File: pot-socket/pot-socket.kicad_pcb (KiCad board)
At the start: 2 copper layers, 18 x 20 mm, 2 parts, among them J1 Conn_01x03

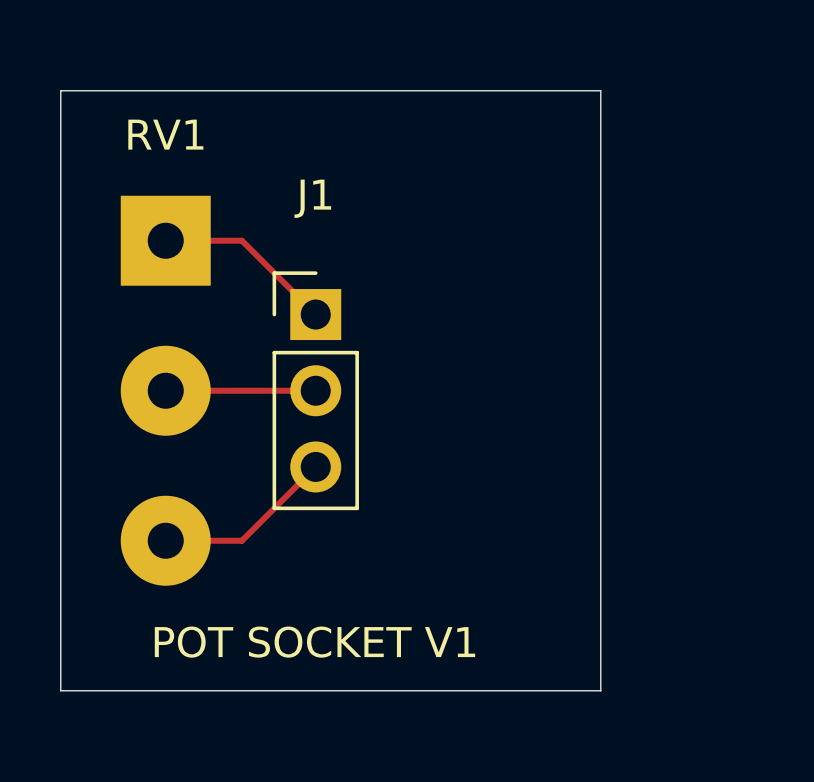
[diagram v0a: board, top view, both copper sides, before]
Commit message: Freecad design for pot socket
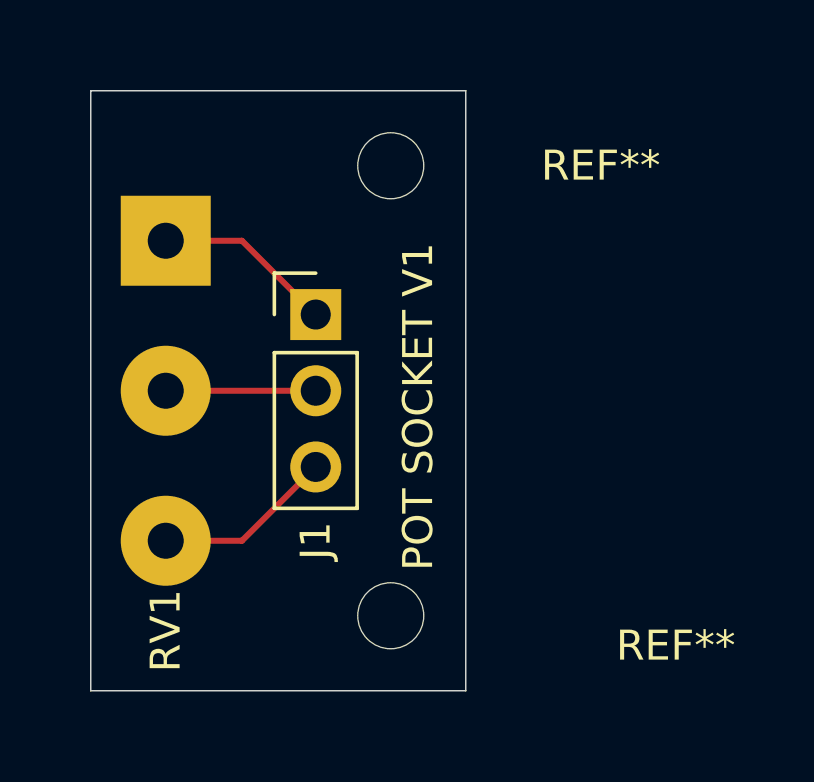
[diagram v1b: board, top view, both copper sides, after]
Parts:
- added REF**: MountingHole_2.2mm_M2, MountingHole:MountingHole_2.2mm_M2, F.Cu at (152.5, 92.5)
- added REF**: MountingHole_2.2mm_M2, MountingHole:MountingHole_2.2mm_M2, F.Cu at (152.5, 107.5)
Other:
- board size 18 x 20 mm -> 12.5 x 20 mm
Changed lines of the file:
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@@
 		(tags "Potentiometer horizontal Alps RK163 Single")
 		(property "Reference" "RV1"
-			(at 0 -3.5 180)
+			(at 0 13 270)
 			(layer "F.SilkS")
 			(effects
@@
 			)
 		)
+	)
+	(footprint "MountingHole:MountingHole_2.2mm_M2"
+		(layer "F.Cu")
+		(at 152.5 92.5)
+		(descr "Mounting Hole 2.2mm, M2, no annular, generated by kicad-footprint-generator mountinghole.py")
+		(tags "mountinghole M2")
+		(property "Reference" "REF**"
+			(at 7 0 0)
+			(layer "F.SilkS")
+			(effects
+				(font
+					(size 1 1)
+					(thickness 0.15)
+				)
+			)
+		)
+		(property "Value" "MountingHole_2.2mm_M2"
+			(at 0 3.15 0)
+			(layer "F.Fab")
+			(effects
+				(font
+					(size 1 1)
+					(thickness 0.15)
+				)
+			)
+		)
+		(property "Datasheet" ""
+			(at 0 0 0)
+			(layer "F.Fab")
+			(hide yes)
+			(effects
+				(font
+					(size 1.27 1.27)
+					(thickness 0.15)
+				)
+			)
+		)
+		(property "Description" ""
+			(at 0 0 0)
+			(layer "F.Fab")
+			(hide yes)
+			(effects
+				(font
+					(size 1.27 1.27)
+					(thickness 0.15)
+				)
+			)
+		)
+		(attr exclude_from_pos_files exclude_from_bom)
+		(fp_circle
+			(center 0 0)
+			(end 2.2 0)
+			(stroke
+				(width 0.15)
+				(type solid)
+			)
+			(fill no)
+			(layer "Cmts.User")
+		)
+		(fp_circle
+			(center 0 0)
+			(end 2.45 0)
+			(stroke
+				(width 0.05)
+				(type solid)
+			)
+			(fill no)
+			(layer "F.CrtYd")
+		)
+		(fp_text user "${REFERENCE}"
+			(at 0 0 0)
+			(layer "F.Fab")
+			(effects
+				(font
+					(size 1 1)
+					(thickness 0.15)
+				)
+			)
+		)
+		(pad "" np_thru_hole circle
+			(at 0 0)
+			(size 2.2 2.2)
+			(drill 2.2)
+			(layers "*.Cu" "*.Mask")
+		)
+		(embedded_fonts no)
 	)
 	(footprint "Connector_PinHeader_2.54mm:PinHeader_1x03_P2.54mm_Vertical"
@@
 		(tags "Through hole pin header THT 1x03 2.54mm single row")
 		(property "Reference" "J1"
-			(at 0 -3.96 0)
+			(at 0 7.54 90)
 			(layer "F.SilkS")
 			(effects
@@
 		)
 	)
+	(footprint "MountingHole:MountingHole_2.2mm_M2"
+		(layer "F.Cu")
+		(at 152.5 107.5)
+		(descr "Mounting Hole 2.2mm, M2, no annular, generated by kicad-footprint-generator mountinghole.py")
+		(tags "mountinghole M2")
+		(property "Reference" "REF**"
+			(at 9.5 1 0)
+			(layer "F.SilkS")
+			(effects
+				(font
+					(size 1 1)
+					(thickness 0.15)
+				)
+			)
+		)
+		(property "Value" "MountingHole_2.2mm_M2"
+			(at 0 3.15 0)
+			(layer "F.Fab")
+			(effects
+				(font
+					(size 1 1)
+					(thickness 0.15)
+				)
+			)
+		)
+		(property "Datasheet" ""
+			(at 0 0 0)
+			(layer "F.Fab")
+			(hide yes)
+			(effects
+				(font
+					(size 1.27 1.27)
+					(thickness 0.15)
+				)
+			)
+		)
+		(property "Description" ""
+			(at 0 0 0)
+			(layer "F.Fab")
+			(hide yes)
+			(effects
+				(font
+					(size 1.27 1.27)
+					(thickness 0.15)
+				)
+			)
+		)
+		(attr exclude_from_pos_files exclude_from_bom)
+		(fp_circle
+			(center 0 0)
+			(end 2.2 0)
+			(stroke
+				(width 0.15)
+				(type solid)
+			)
+			(fill no)
+			(layer "Cmts.User")
+		)
+		(fp_circle
+			(center 0 0)
+			(end 2.45 0)
+			(stroke
+				(width 0.05)
+				(type solid)
+			)
+			(fill no)
+			(layer "F.CrtYd")
+		)
+		(fp_text user "${REFERENCE}"
+			(at 0 0 0)
+			(layer "F.Fab")
+			(effects
+				(font
+					(size 1 1)
+					(thickness 0.15)
+				)
+			)
+		)
+		(pad "" np_thru_hole circle
+			(at 0 0)
+			(size 2.2 2.2)
+			(drill 2.2)
+			(layers "*.Cu" "*.Mask")
+		)
+		(embedded_fonts no)
+	)
 	(gr_rect
-		(start 141.5 90)
-		(end 159.5 110)
+		(start 142.5 90)
+		(end 155 110)
 		(stroke
 			(width 0.05)
@@
 	)
 	(gr_text "POT SOCKET V1"
-		(at 144.5 109 0)
+		(at 154 106 90)
 		(layer "F.SilkS")
 		(effects

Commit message: Update pot socket model
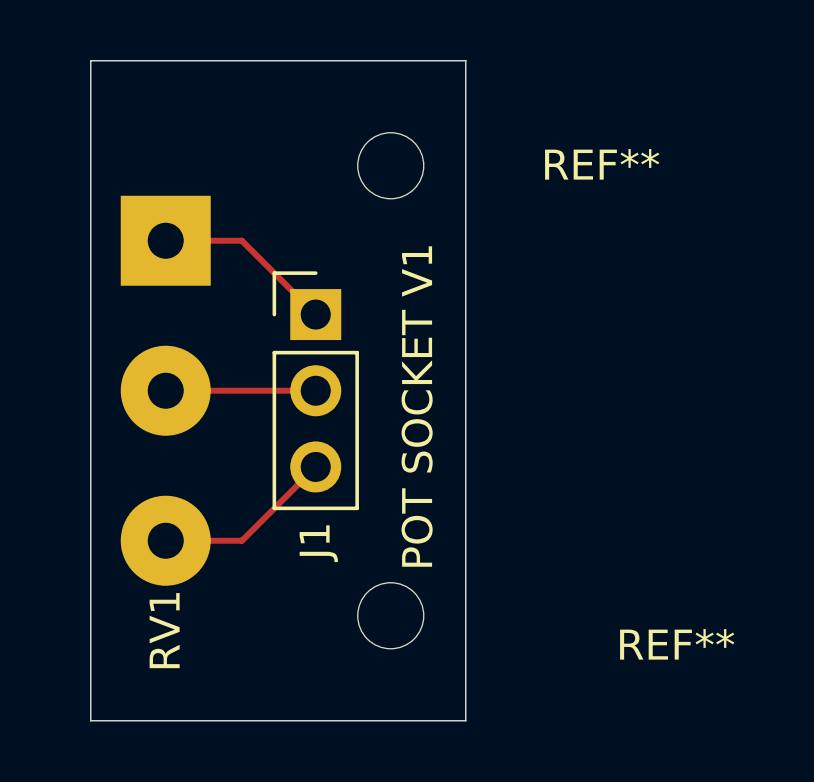
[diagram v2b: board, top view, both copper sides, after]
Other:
- board size 12.5 x 20 mm -> 12.5 x 22 mm
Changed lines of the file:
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@@
 	)
 	(gr_rect
-		(start 142.5 90)
-		(end 155 110)
+		(start 142.5 89)
+		(end 155 111)
 		(stroke
 			(width 0.05)

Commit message: Update pot socket pcb
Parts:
- moved RV1 2.50 mm to (147.5, 95.0)
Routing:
- net Net-(J1-Pin_3): track 6.02 -> 3.52 mm
- net Net-(J1-Pin_1): track 6.02 -> 3.52 mm
- net Net-(J1-Pin_2): track 5.00 -> 2.50 mm
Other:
- board size 12.5 x 22 mm -> 10.5 x 22 mm
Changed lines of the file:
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@@
 	(footprint "Potentiometer_THT:Potentiometer_Alps_RK163_Single_Horizontal"
 		(layer "F.Cu")
-		(at 145 95)
+		(at 147.5 95)
 		(descr "1110U1Q 1110TNP 1110U2A 1110U0Q Potentiometer, horizontal, Alps RK163 Single, https://tech.alpsalpine.com/prod/e/pdf/potentiometer/rotarypotentiometers/rk16/rk16.pdf")
 		(tags "Potentiometer horizontal Alps RK163 Single")
 		(property "Reference" "RV1"
-			(at 0 13 270)
+			(at 0 13.5 270)
 			(layer "F.SilkS")
 			(effects
@@
 		(attr through_hole)
 		(fp_line
-			(start -1.38 -1.38)
-			(end 0 -1.38)
-			(stroke
-				(width 0.12)
-				(type solid)
-			)
-			(layer "F.SilkS")
-		)
-		(fp_line
-			(start -1.38 0)
-			(end -1.38 -1.38)
-			(stroke
-				(width 0.12)
-				(type solid)
-			)
-			(layer "F.SilkS")
-		)
-		(fp_line
-			(start -1.38 1.27)
-			(end -1.38 6.46)
-			(stroke
-				(width 0.12)
-				(type solid)
-			)
-			(layer "F.SilkS")
-		)
-		(fp_line
-			(start -1.38 1.27)
-			(end 1.38 1.27)
-			(stroke
-				(width 0.12)
-				(type solid)
-			)
-			(layer "F.SilkS")
-		)
-		(fp_line
-			(start -1.38 6.46)
-			(end 1.38 6.46)
-			(stroke
-				(width 0.12)
-				(type solid)
-			)
-			(layer "F.SilkS")
-		)
-		(fp_line
-			(start 1.38 1.27)
-			(end 1.38 6.46)
-			(stroke
-				(width 0.12)
-				(type solid)
-			)
-			(layer "F.SilkS")
-		)
-		(fp_line
 			(start -1.77 -1.77)
 			(end -1.77 6.85)
@@
 			)
 			(layer "F.CrtYd")
-		)
-		(fp_line
-			(start -1.27 -0.635)
-			(end -0.635 -1.27)
-			(stroke
-				(width 0.1)
-				(type solid)
-			)
-			(layer "F.Fab")
-		)
-		(fp_line
-			(start -1.27 6.35)
-			(end -1.27 -0.635)
-			(stroke
-				(width 0.1)
-				(type solid)
-			)
-			(layer "F.Fab")
-		)
-		(fp_line
-			(start -0.635 -1.27)
-			(end 1.27 -1.27)
-			(stroke
-				(width 0.1)
-				(type solid)
-			)
-			(layer "F.Fab")
-		)
-		(fp_line
-			(start 1.27 -1.27)
-			(end 1.27 6.35)
-			(stroke
-				(width 0.1)
-				(type solid)
-			)
-			(layer "F.Fab")
-		)
-		(fp_line
-			(start 1.27 6.35)
-			(end -1.27 6.35)
-			(stroke
-				(width 0.1)
-				(type solid)
-			)
-			(layer "F.Fab")
 		)
 		(fp_text user "${REFERENCE}"
@@
 	)
 	(gr_rect
-		(start 142.5 89)
+		(start 144.5 89)
 		(end 155 111)
 		(stroke
@@
 	(segment
 		(start 147.54 105)
-		(end 150 102.54)
+		(end 147.5 105)
 		(width 0.2)
 		(layer "F.Cu")
@@
 	)
 	(segment
-		(start 145 105)
+		(start 150 102.54)
 		(end 147.54 105)
 		(width 0.2)
@@
 	)
 	(segment
-		(start 145 100)
-		(end 150 100)
+		(start 150 100)
+		(end 147.5 100)
 		(width 0.2)
 		(layer "F.Cu")
@@
 	)
 	(segment
-		(start 147.54 95)
-		(end 150 97.46)
+		(start 150 97.46)
+		(end 149.96 97.46)
 		(width 0.2)
 		(layer "F.Cu")
@@
 	)
 	(segment
-		(start 145 95)
-		(end 147.54 95)
+		(start 149.96 97.46)
+		(end 147.5 95)
 		(width 0.2)
 		(layer "F.Cu")
